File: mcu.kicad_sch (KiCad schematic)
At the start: 14 parts, among them J3 DevKit J1, J4 DevKit J3, J5 I2C / Qwiic, J6 WS2812, J7 Rail break-out, U2 74AHCT1G125

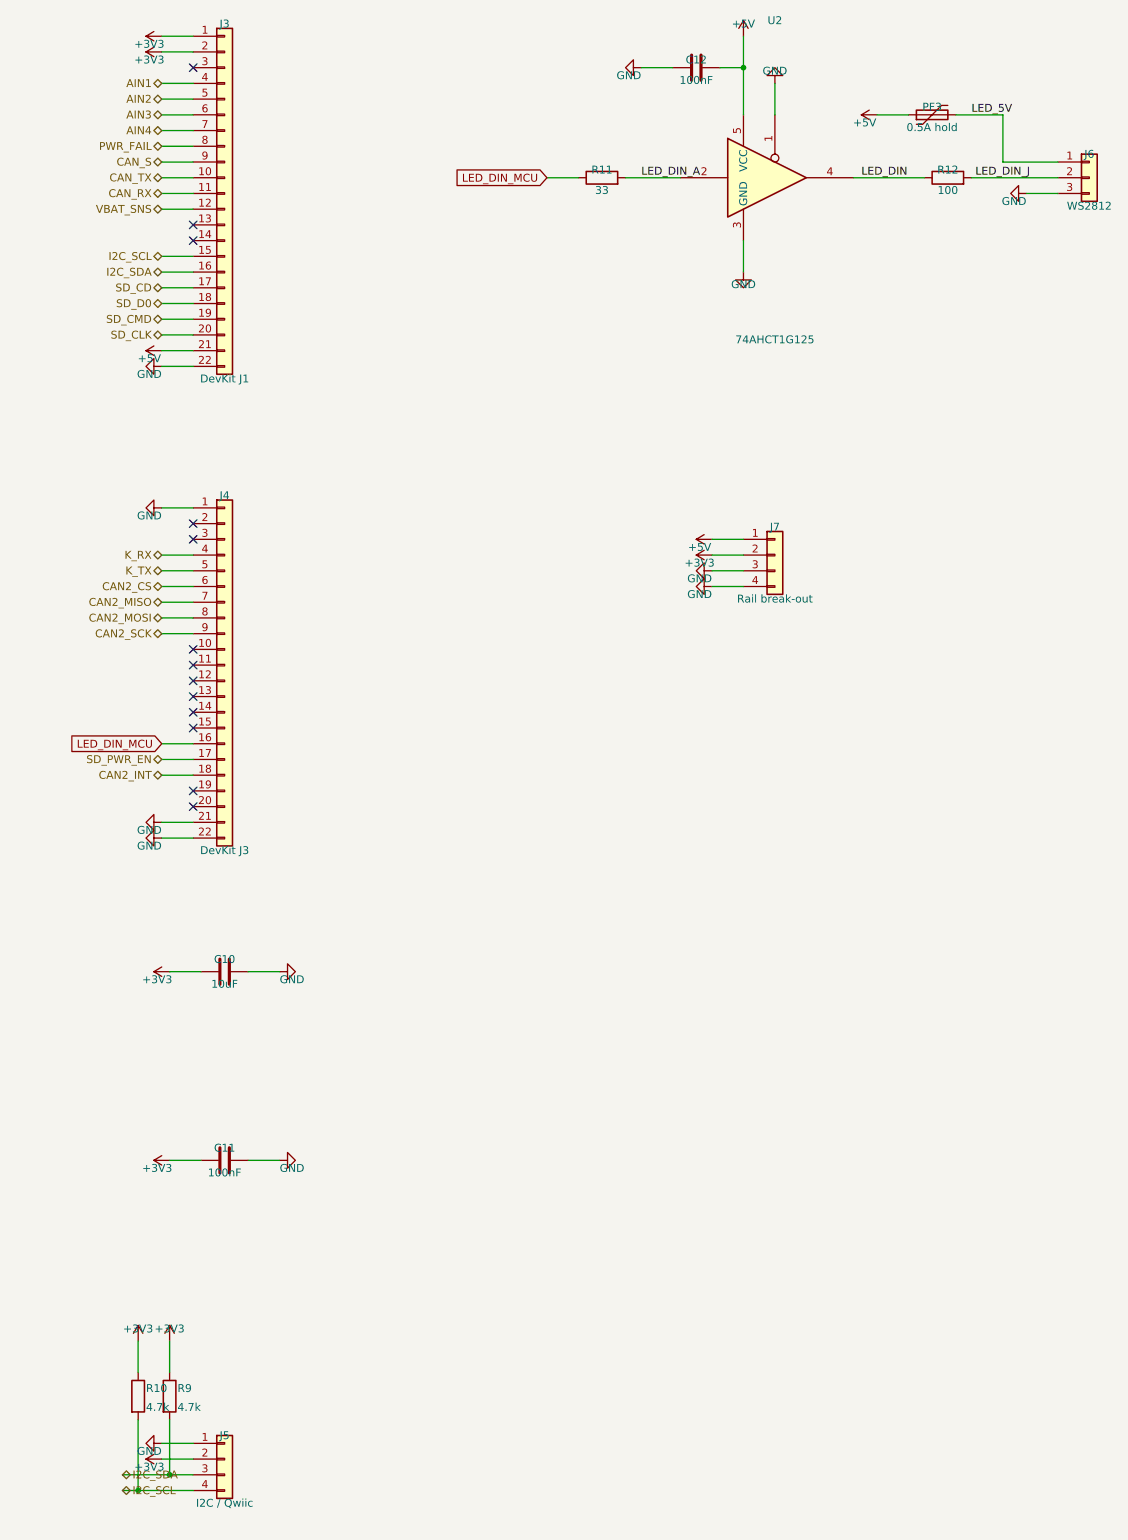
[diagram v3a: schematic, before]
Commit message: Make the schematic readable: wire the loose parts, stop text printing through symbols
Three things the drawing was doing badly, all now measured by a new
gen/audit_schematic.py rather than judged by eye.

LOOSE PARTS ARE WIRED NOW. A decoupling capacitor is a two-pin part with a
rail on each pin, and the column packer had no reason to put one next to
another -- so each came out as its own island with a net label at both ends,
twenty-odd of them down the edge of the power sheet. Electrically perfect,
visually a parts bin. build_ladders() groups the leftovers by which pair of
nets they sit across and draws each group as a proper ladder: one wire along
the top pins, one along the bottom, a junction at every rung and a power
symbol at each end. Nine groups across five sheets, including the supercap
bank and the battery monitor, and it removes two labels per part.

Grouping is on the actual pin GEOMETRY, not the symbol name, which is what
lets a balancing resistor share a ladder with the capacitor it balances while
keeping out a TVS diode whose pins are 1.3 mm closer together -- that one ERC
caught as two unconnected wire endpoints.

TEXT NO LONGER PRINTS THROUGH SYMBOLS. The offsets that place a reference and
a value work from the box around a part's PINS, and a symbol's graphic is
routinely drawn outside it. A power symbol's arrow therefore went straight
through its own name -- "+5VS" read "+2VS" at a glance, which is exactly how
somebody ends up probing the wrong rail -- and a capacitor lying on its side
has a y extent of exactly zero, so its reference and value printed across the
plates. Both now work from a floor on the body size. Rail names are also
centred on their own pin instead of drooping half a pitch onto the next one,
and the solder jumpers lost "(default OFF)" from their value into their note,
which is eighteen characters of text on a part 1.3 mm wide.

THE HAND-DRAWN BLOCKS WERE RE-SPACED to suit, because their tables were laid
out when the text sat closer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
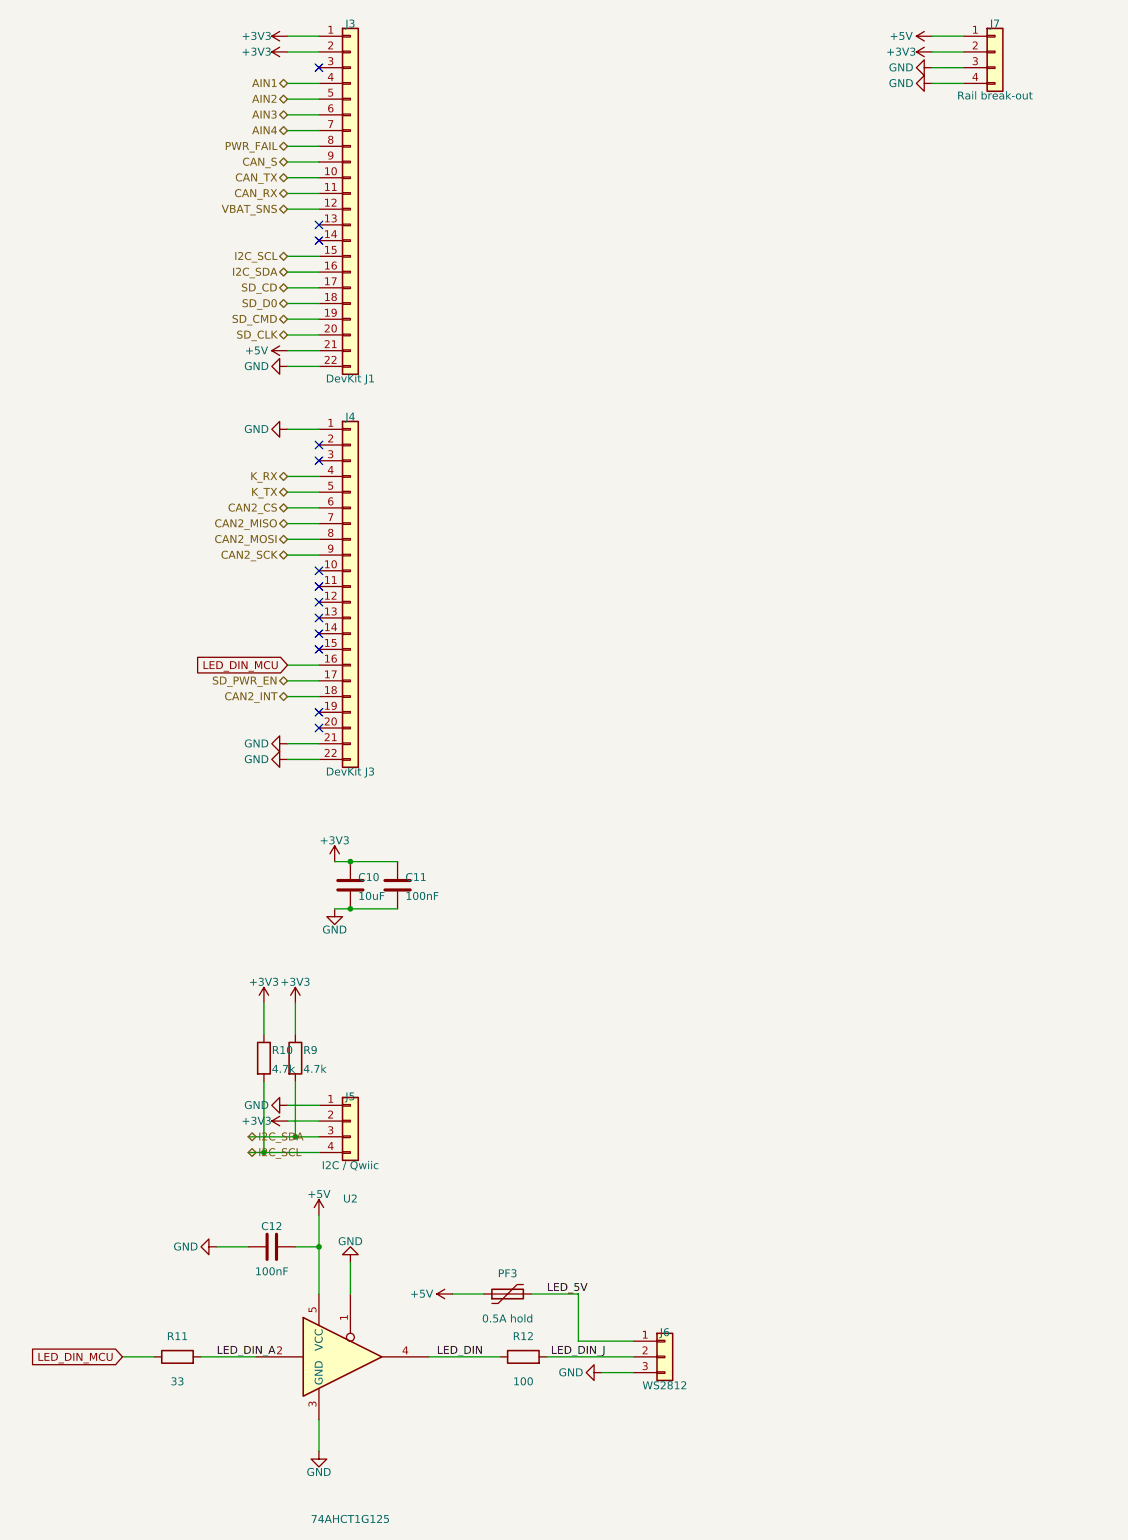
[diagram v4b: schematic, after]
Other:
- moved on the sheet: C10, C11, C12, J3, J4, J5, J6, J7, PF3, R10, R11, R12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
